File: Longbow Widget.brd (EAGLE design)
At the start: 27.4 x 18 mm, 12 parts, among them X1 87832-14

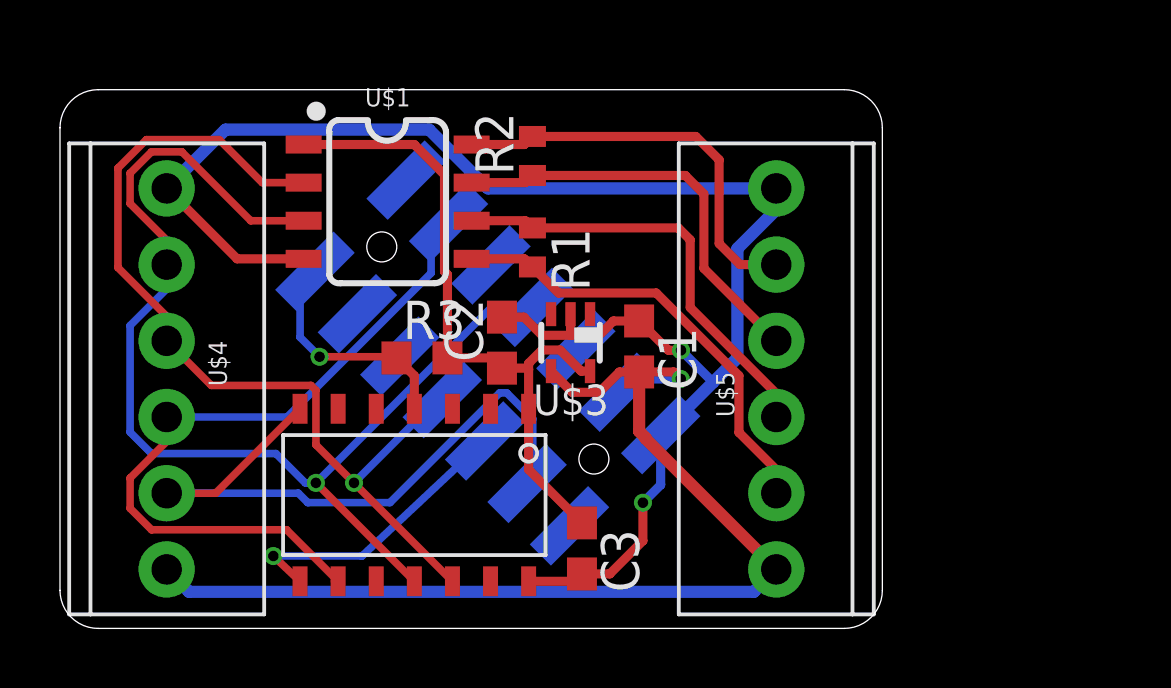
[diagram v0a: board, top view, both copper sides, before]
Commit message: Updated Longbow Widget schematic, very preliminary board layout
Added fixes for many of the issues to the schematic, made very preliminary board layout

Likely to add some kind of transient protection to Longbow Widget, have left space on preliminary board layout to add in later
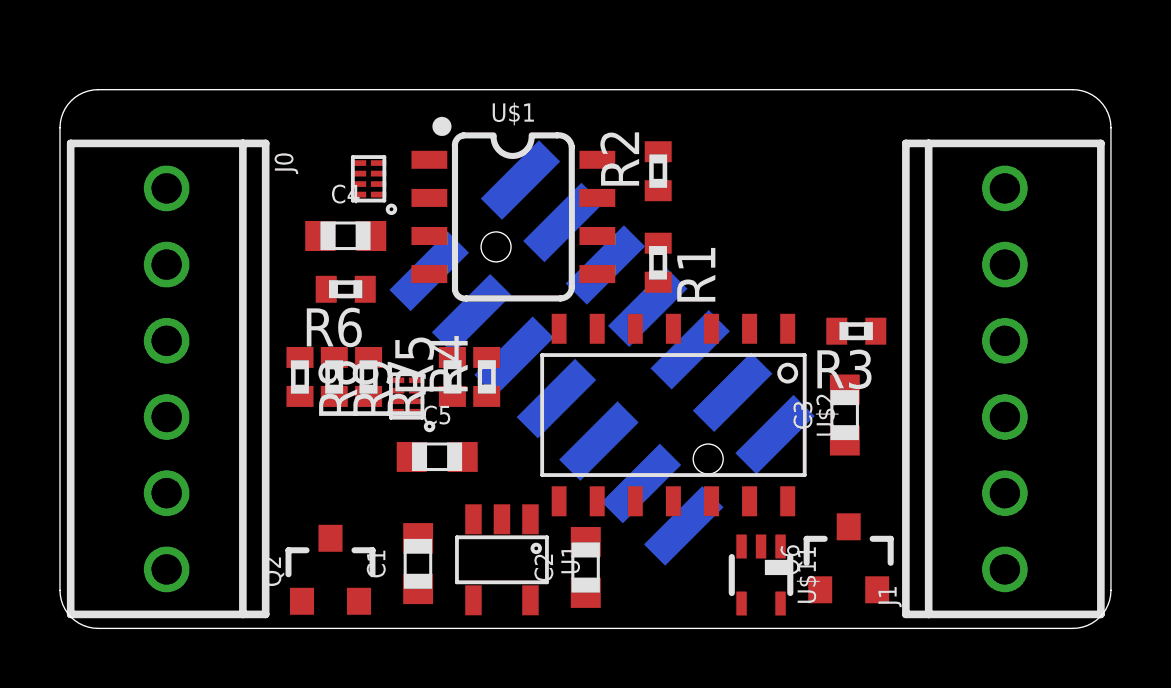
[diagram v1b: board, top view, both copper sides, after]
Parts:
- removed U$4, U$5: CONN_6SCREW_2.54, bschulz:1X06
- removed X1: 87832-14, bschulz:87832-14
- added C4, C5: 0.1uF, bschulz_passives:C0603
- added J0, J1: CONN_6SCREW_2.54, bschulz:1X06_SCREW
- added J2: 87832-14, bschulz:87832-14
- added Q2: DMG3404, bschulz:SOT23-3
- added Q6: FDN360P, bschulz:SOT23-3
- added R4, R5, R8, R9: 10k, bschulz_passives:R0402
- added R6, R7: 200k, bschulz_passives:R0402
- added U$11: MIC842H, bschulz:DCK_R-PDSO-G5
- added U$6: LSF0102DQE, bschulz:DQE_R-PX2SON-N8
- added U1: TPS7A0533DBV, bschulz:SOT23-5
- C1: value 0.1uF -> 1uF
- C2: value 0.47uF -> 1uF
- R1, R2: value (none) -> 100R
- R3: device bschulz_passives:R0603 -> bschulz_passives:R0402
- U$3: value TPS79733 -> LSF0102DQE; device bschulz:DCK_R-PDSO-G5 -> bschulz:DQE_R-PX2SON-N8
- moved R3 14.5 mm to (31.2, 19.7), turned to 180 degrees
- moved C1 10.3 mm to (16.6, 11.9), turned to 90 degrees
- moved C3 9.83 mm to (30.9, 16.9), turned to 90 degrees
- moved U$2 9.04 mm to (25.1, 16.9)
- moved C2 8.00 mm to (22.2, 11.8)
- moved U$3 5.74 mm to (16.3, 17.5), turned to 90 degrees
- moved R1 4.22 mm to (24.6, 22.0)
- moved R2 4.22 mm to (24.6, 25.0)
- moved U$1 4.22 mm to (19.8, 23.5)
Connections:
- removed net 5V: C1.2, U$3.4, U$4.6, U$5.1, X1.4
- new net 3V3_CTRL: U$11.1, U$2.5
- new net GND1: Q2.2
- new net N$1: C5.1, R7.1, U$3.7, U$3.8
- new net N$3: C4.1, R6.1, U$6.7, U$6.8
- new net N$4: Q6.1, U$11.4
- new net RX_HV: J0.1, U$6.5
- new net SCL_HV: J0.3, R8.1, U$3.5
- new net SDA_HV: J0.4, R9.1, U$3.6
- new net TX_HV: J0.2, U$6.6
- new net VIN+: C1.2, J0.5, J2.4, Q2.1, Q6.2, R6.2, R7.2, R8.2, R9.2, U$11.5, U1.1, U1.3
- new net VIN-: J0.6, Q2.3
- new net VOUT: J1.1, Q6.3
- net /RESET: now also J2.13; no longer X1.13
- net 3V3: now also R4.2, R5.2, U$3.2, U$6.2, U1.5; no longer U$3.5
- net GND: now also C4.2, C5.2, J1.6, J2.2, U$11.2, U$3.1, U$6.1, U1.2; no longer U$3.2, U$4.1, U$5.6, X1.2
- net MISO: now also J2.5; no longer X1.5
- net RX: now also J2.8, U$2.12, U$6.4; no longer U$2.11, U$4.2, X1.8
- net RX+: now also J1.5; no longer U$5.5
- net RX-: now also J1.4; no longer U$5.4
- net SCL: now also J2.12, R4.1, U$3.4; no longer U$4.4, X1.12
- net SDA: now also J2.3, R5.1, U$3.3; no longer U$4.5, X1.3
- net TX: now also J2.7, U$2.11, U$6.3; no longer U$2.12, U$4.3, X1.7
- net TX+: now also J1.2; no longer U$5.2
- net TX-: now also J1.3; no longer U$5.3
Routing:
- net GND: track 54.5 -> 0.00 mm, vias 2 -> 0
- net RX: track 37.9 -> 0.00 mm, vias 1 -> 0
- net 5V: track 36.7 -> 0.00 mm, vias 1 -> 0
- net TX: track 31.6 -> 0.00 mm, vias 1 -> 0
- net SCL: track 24.5 -> 0.00 mm
- net 3V3: track 22.7 -> 0.00 mm
- net SDA: track 22.2 -> 0.00 mm
- net TX+: track 15.0 -> 0.00 mm
- net TX-: track 14.6 -> 0.00 mm
- net RX-: track 14.0 -> 0.00 mm
- net RX+: track 13.7 -> 0.00 mm
- net MISO: track 9.78 -> 0.00 mm, vias 1 -> 0
- net /RESET: track 8.08 -> 0.00 mm, vias 1 -> 0
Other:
- board size 27.4 x 18 mm -> 35 x 18 mm

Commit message: Preliminary layout for Longbow Widget complete
Needs cleanup and changes to silk screen before review, should be nearly functional (should add polygon pours for power on input side). Also added preliminary BOM, which requires update with new parts and after adding additional part numbers (for pulse proof resistors, snub resistors, etc)
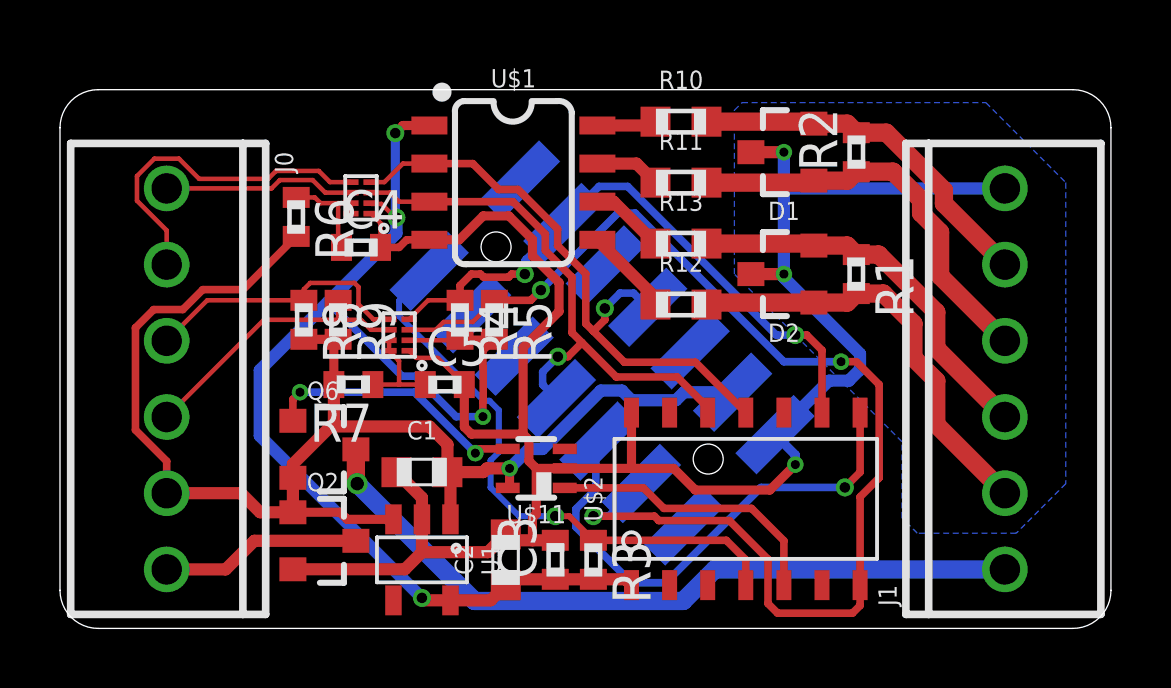
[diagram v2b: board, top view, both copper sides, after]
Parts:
- added D1, D2: (no value), bschulz:SOT23-3
- added R10, R11, R12, R13: 10R, bschulz_passives:R0603
- C3, C4, C5: device bschulz_passives:C0603 -> bschulz_passives:C0402
- moved Q6 17.9 mm to (13.5, 15.7), turned to 270 degrees
- moved R3 11.6 mm to (22.5, 12.1), turned to 270 degrees
- moved C3 10.8 mm to (21.2, 12.1)
- moved U$11 8.29 mm to (20.6, 15.1), turned to 90 degrees
- moved R2 6.63 mm to (31.2, 25.7)
- moved R1 6.61 mm to (31.2, 21.6)
- moved U$2 3.69 mm to (27.6, 14.1), turned to 0 degrees
- moved C1 3.05 mm to (16.8, 15.0), turned to 0 degrees
- moved R6 2.92 mm to (12.6, 23.5), turned to 270 degrees
- moved C2 2.68 mm to (19.6, 12.1)
- moved U1 2.67 mm to (16.8, 12.1)
- moved C5 2.43 mm to (17.5, 17.9)
- moved R5 2.36 mm to (19.2, 20.1), turned to 270 degrees
- moved R4 2.10 mm to (18.0, 20.1), turned to 270 degrees
- moved U$3 2.05 mm to (16.0, 19.6)
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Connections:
- removed net GND1: Q2.2
- new net N$2: R10.1, U$1.8
- new net N$5: R11.1, U$1.7
- new net N$6: R12.1, U$1.5
- new net N$7: R13.1, U$1.6
- net GND: now also D1.3, D2.3, Q2.2
- net RX: now also J2.7, U$6.3; no longer J2.8, U$6.4
- net RX+: now also D1.2, R10.2; no longer U$1.8
- net RX-: now also D1.1, R11.2; no longer U$1.7
- net RX_HV: now also U$6.6; no longer U$6.5
- net TX: now also J2.8, U$6.4; no longer J2.7, U$6.3
- net TX+: now also D2.1, R12.2; no longer U$1.5
- net TX-: now also D2.2, R13.2; no longer U$1.6
- net TX_HV: now also U$6.5; no longer U$6.6
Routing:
- net GND: track 0.00 -> 70.4 mm, vias 0 -> 3
- net VIN+: track 0.00 -> 46.6 mm, vias 0 -> 1
- net 3V3: track 0.00 -> 41.7 mm, vias 0 -> 4
- net SDA: track 0.00 -> 40.5 mm, vias 0 -> 3
- net VOUT: track 0.00 -> 24.8 mm, vias 0 -> 1
- net SCL: track 0.00 -> 20.6 mm, vias 0 -> 2
- net TX: track 0.00 -> 20.2 mm, vias 0 -> 1
- net /RESET: track 0.00 -> 19.6 mm, vias 0 -> 1
- net RX: track 0.00 -> 18.6 mm, vias 0 -> 1
- net MISO: track 0.00 -> 16.9 mm, vias 0 -> 1
- net TX+: track 0.00 -> 14.4 mm
- net RX-: track 0.00 -> 13.6 mm
- net TX-: track 0.00 -> 13.0 mm
- net RX+: track 0.00 -> 12.2 mm
- net TX_HV: track 0.00 -> 11.3 mm
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- added copper zone on layer 16, net GND

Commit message: Cleaned up Widget
Cleaned up layout of widget, adjusted silkscreen, fixed pinout issue, generated final gerbers, ready for prototype
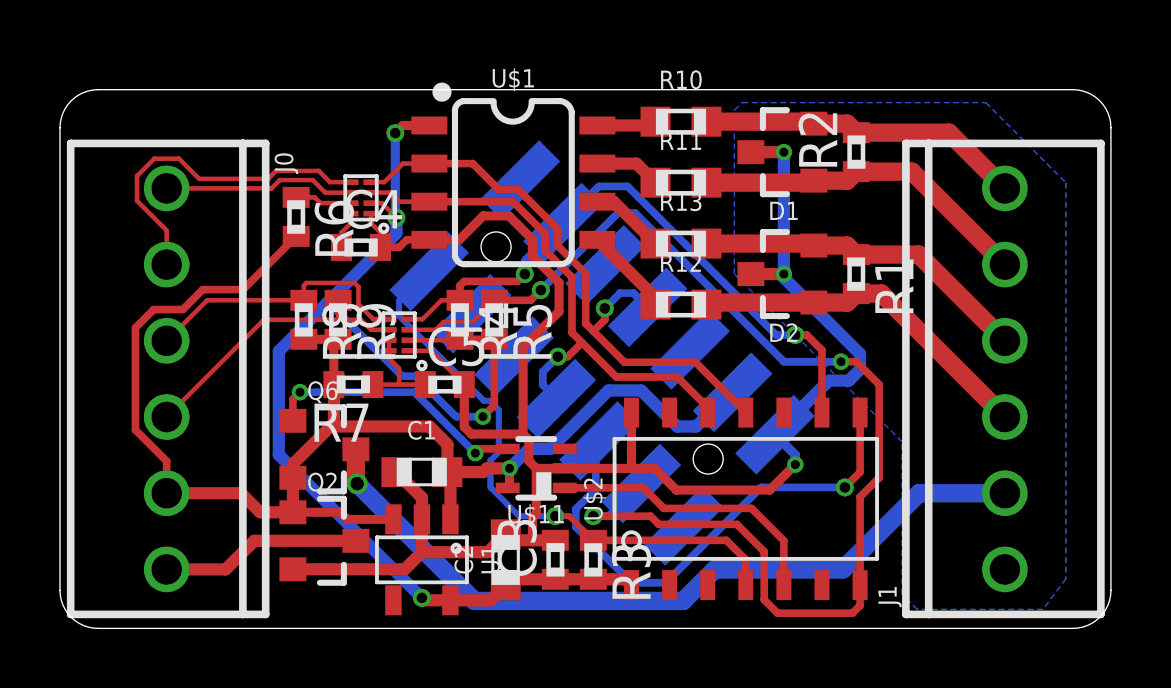
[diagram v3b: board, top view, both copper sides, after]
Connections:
- net GND: now also J1.1; no longer J1.6
- net RX+: now also J1.6; no longer J1.5
- net RX-: now also J1.5; no longer J1.4
- net TX+: now also J1.3; no longer J1.2
- net TX-: now also J1.4; no longer J1.3
- net VOUT: now also J1.2; no longer J1.1
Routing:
- net GND: track 70.4 -> 63.1 mm
- net TX+: track 14.4 -> 11.8 mm
- net RX-: track 13.6 -> 11.4 mm
- net TX-: track 13.0 -> 11.3 mm
- net RX+: track 12.2 -> 10.9 mm
- net VOUT: track 24.8 -> 25.9 mm
- net VIN+: track 46.6 -> 47.3 mm
- net 3V3: track 41.7 -> 41.1 mm
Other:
- board text added: "Vin"
- board text added: "Vout"
- board text added: "±"
- board text removed: "5V"

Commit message: Final designs for Longbow Widget v0.1 and Universal Breakout Pogo board
Added final design (minor silk screen additions) of the Longbow widget, also designed a modified Universal breakout which has support for pogo pins. Generated final gerbers for both as well
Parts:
- added FRAME1: (no value), bschulz:CREATIVE_COMMONS
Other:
- board text added: "3.3v ~ 5v"
- board text added: "To Logger"
- board text added: "To Sensor"
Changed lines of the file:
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@@
 <text x="39.37" y="16.51" size="0.8128" layer="52" font="vector" ratio="16" rot="MR0">TX+</text>
 <text x="39.37" y="13.97" size="0.8128" layer="52" font="vector" ratio="16" rot="MR0">Vout</text>
-<text x="28.194" y="19.431" size="0.8128" layer="122" font="vector" ratio="16" rot="MR45">Northern Widget
+<text x="28.194" y="19.431" size="0.8128" layer="52" font="vector" ratio="16" rot="MR45">Northern Widget
 Bobby Schulz</text>
 <wire x1="9.398" y1="14.986" x2="10.795" y2="13.589" width="0.254" layer="52" curve="-95.452622"/>
@@
 <text x="9.906" y="12.954" size="1.27" layer="52" font="vector" ratio="15" rot="MR0" align="center">±</text>
 <wire x1="10.795" y1="13.589" x2="10.795" y2="12.319" width="0.254" layer="52"/>
+<text x="36.195" y="26.4795" size="0.8128" layer="52" font="vector" ratio="15" rot="MR0" align="center">To Sensor</text>
+<text x="8.255" y="26.4795" size="0.8128" layer="52" font="vector" ratio="15" rot="MR0" align="center">To Logger</text>
+<text x="10.287" y="20.701" size="0.8128" layer="52" font="vector" ratio="15" rot="MR270" align="center">3.3v ~ 5v</text>
 </plain>
 <attributes>
@@
 <attribute name="VALUE_PART" value="" x="25.4" y="22.606" size="1.778" layer="27" display="off"/>
 </element>
+<element name="FRAME1" library="bschulz" package="CREATIVE_COMMONS" value="" x="-29.89530625" y="0">
+<attribute name="DESIGNER" value="Bobby Schulz" x="-29.89530625" y="0" size="1.778" layer="27" display="off"/>
+<attribute name="PROJECT" value="Longbow" x="-29.89530625" y="0" size="1.778" layer="27" display="off"/>
+<attribute name="REV" value="v0.1" x="-29.89530625" y="0" size="1.778" layer="27" display="off"/>
+</element>
 </elements>

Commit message: Fixed part numbers on Longbow Widget, generated new BOMs
Parts list is updated and fully auto generating
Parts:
- J2: value 87832-14 -> 87832-14MALE
